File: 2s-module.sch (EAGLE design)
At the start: 3 parts, among them J1 CQ-USB-C16PSMT01

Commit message: build balancer prototype
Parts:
- added C1: 1nF, Capacitor:C_CHIP-0603(1608-METRIC)
- added C2: 22uF, Capacitor:C_CHIP-1206(3216-METRIC)
- added C3, C4, C5: 10nF, Capacitor:C_CHIP-0603(1608-METRIC)
- added JP1: PINHD-1X3, Connector:PINHD-1X3
- added L1: 0630CDMCCDS-4R7MC, 0630CDMCCDS-4R7MC:0630CDMCCDS-4R7MC
- added LED1: red, adafruit:LEDCHIPLED_0603
- added R3: 1k, resistor:R-US_R0603
- added R4: 25k, resistor:R-US_R0603
- added U1: MCP4725, SparkFun-IC-Conversion:MCP4725SOT-23
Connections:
- new net BATC: C4.2, C5.1, JP1.2, L1.P$1, LED1.C, U1.AO
- new net BATP: C2.1, C4.1, JP1.1, U1.SCL
- new net BIAS: C3.2, U1.VDD
- new net ISET: C1.2, R4.2, U1.VOUT
- new net N$1: LED1.A, R3.2
- new net SW: C3.1, L1.P$2, R3.1, U1.SDA
- net GND: now also C1.1, C2.2, C5.2, JP1.3, R4.1, U1.VSS
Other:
- note added: "2.2uH"
- note added: "ETA3000"
- moved on the sheet: R2

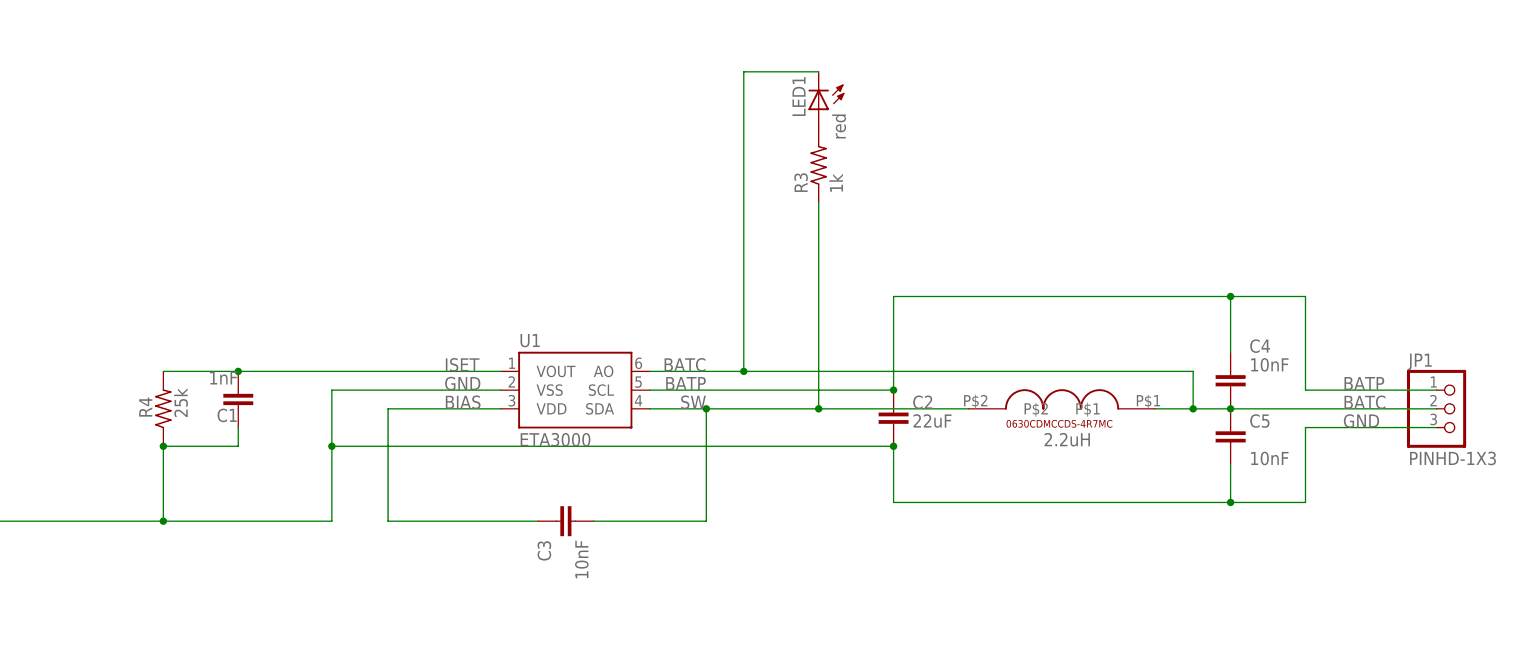
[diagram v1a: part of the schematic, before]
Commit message: add optocoupler
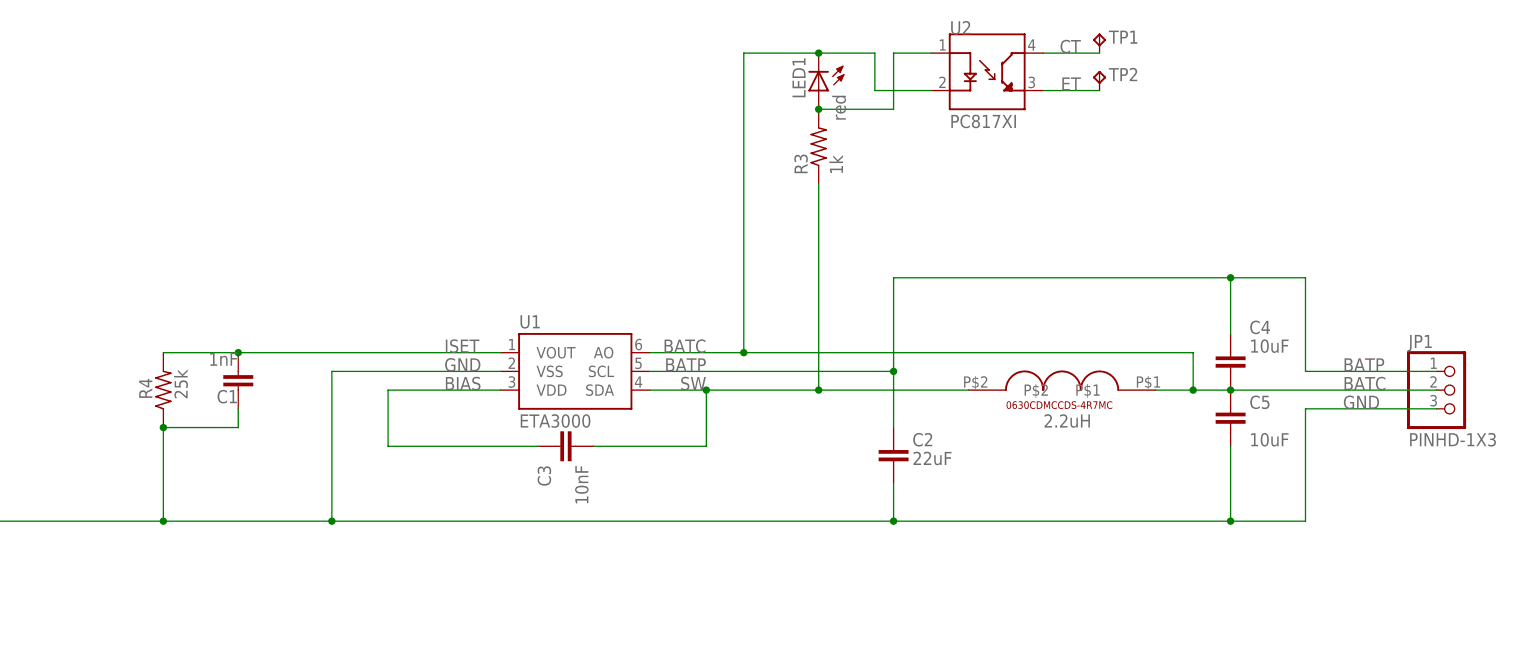
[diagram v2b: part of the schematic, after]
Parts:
- added TP1, TP2: TPB1,27, BeagleBone_Blue_R3:TPB1,27
- added U2: PC817XI, PC817XI:PC817XI
- C4, C5: value 10nF -> 10uF
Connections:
- new net CT: TP1.TP, U2.CT
- new net ET: TP2.TP, U2.ET
- net BATC: now also U2.C
- net N$1: now also U2.A
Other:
- moved on the sheet: C1, C2, C3, C4, C5, JP1, LED1, R3, R4, U1

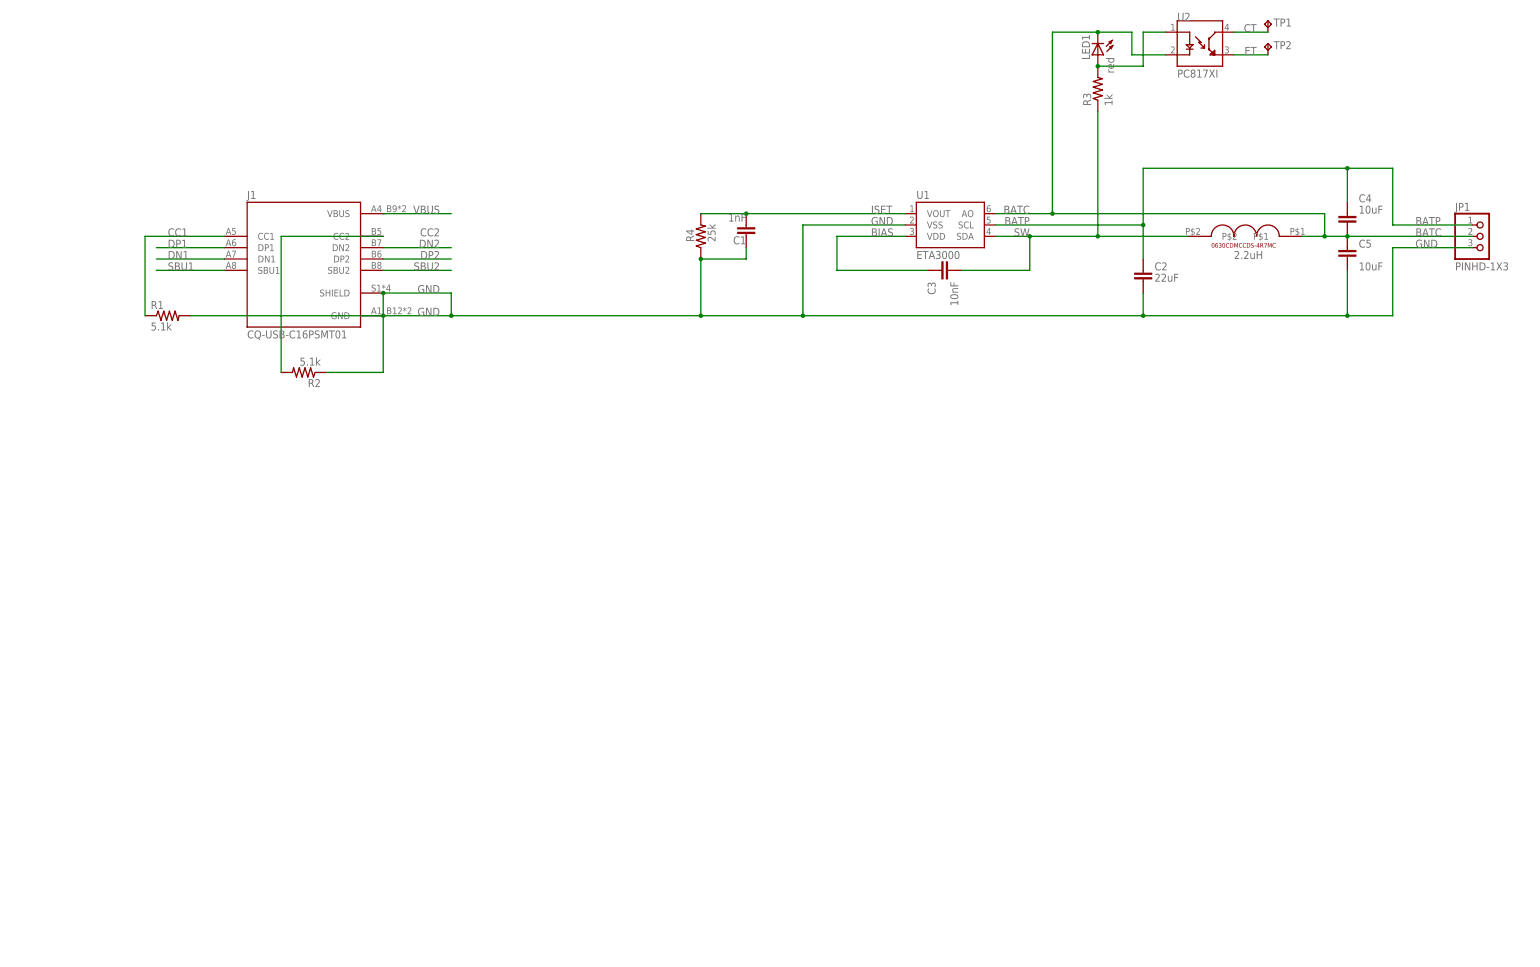
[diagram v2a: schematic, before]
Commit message: finish initial prototype, inductors may change
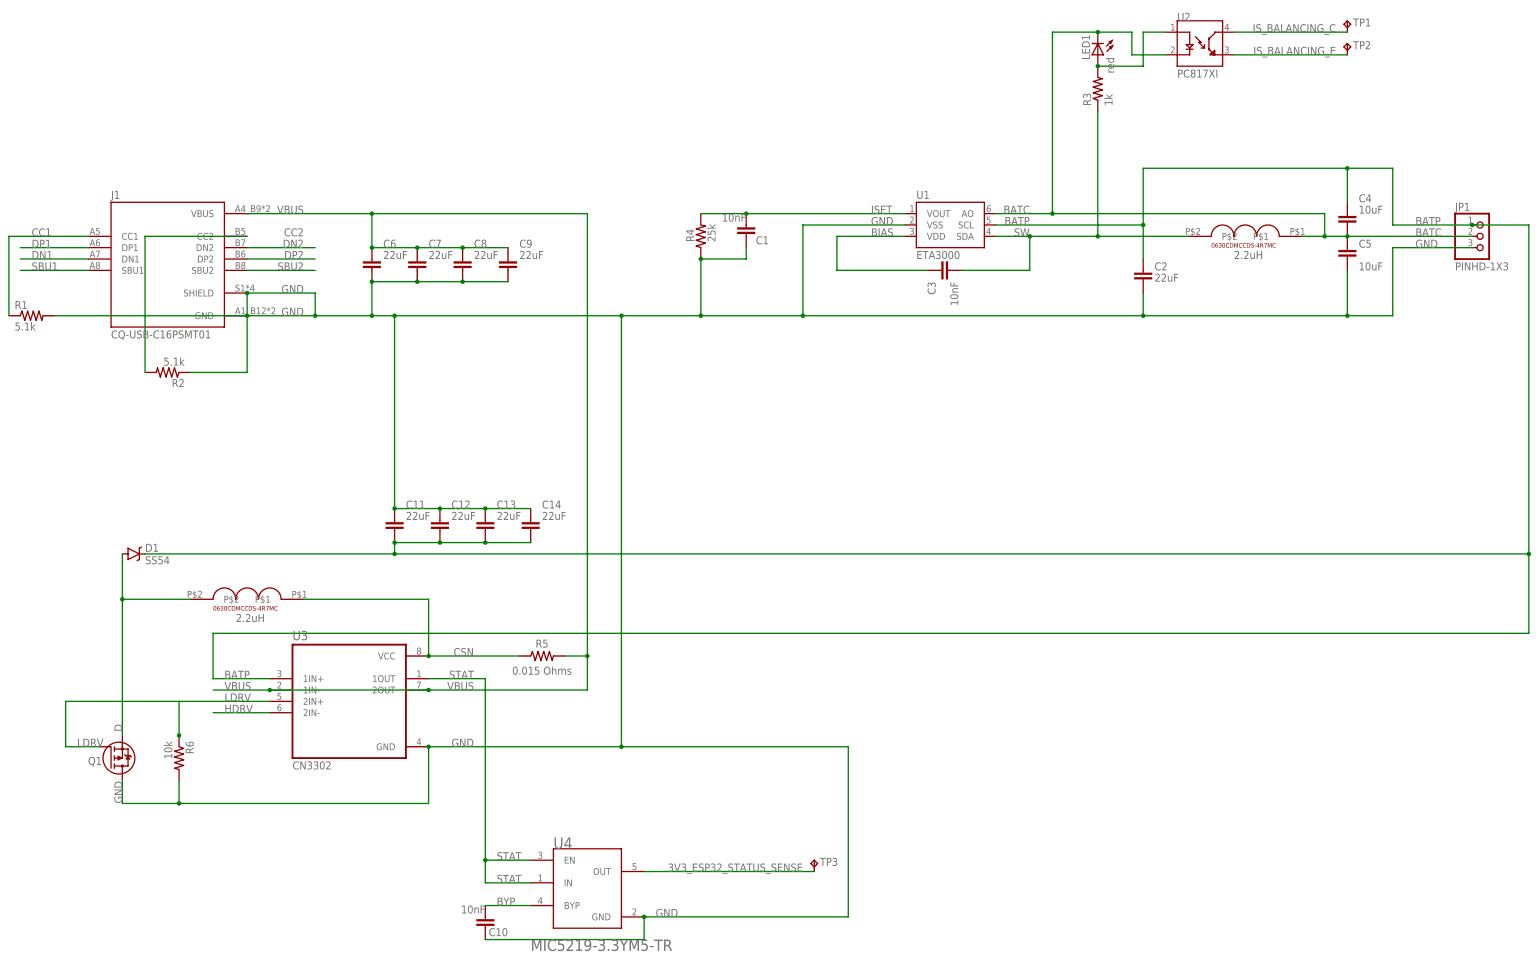
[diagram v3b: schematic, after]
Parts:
- added C10: 10nF, Capacitor:C_CHIP-0603(1608-METRIC)
- added C11, C12, C13, C14, C6, C7, C8, C9: 22uF, Capacitor:C_CHIP-1206(3216-METRIC)
- added D1: SS54, SS54:SS54
- added L2: 0630CDMCCDS-4R7MC, 0630CDMCCDS-4R7MC:0630CDMCCDS-4R7MC
- added Q1: IRFR9020A, semiconductor:IRFR9020A
- added R5: 0.015 Ohms, Resistor:R-US_CHIP-2512(6332-METRIC)
- added R6: 10k, resistor:R-US_R0603
- added TP3: TPB1,27, BeagleBone_Blue_R3:TPB1,27
- added U3: LM393DR, LM393DR:LM393DR
- added U4: MICROCHIP_MIC5219-3_3YM5-TRMICROCHIP_MIC5219-3_3YM5-TR_0_0, Microchip - MIC5219-3.3YM5-TR:MICROCHIP_MIC5219-3_3YM5-TRMICROCHIP_MIC5219-3_3YM5-TR_0_0
- C1: value 1nF -> 10nF
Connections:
- net CT renamed IS_BALANCING_C
- net ET renamed IS_BALANCING_E
- new net 3V3_ESP32_STATUS_SENSE: TP3.TP, U4.OUT
- new net BYP: C10.2, U4.BYP
- new net CSN: L2.P$1, R5.1, U3.VCC
- new net D: D1.A, L2.P$2, Q1.S
- new net HDRV: U3.2IN-
- new net LDRV: Q1.G, R6.1, U3.2IN+
- new net STAT: U3.1OUT, U4.EN, U4.IN
- net BATP: now also C11.2, C12.2, C13.2, C14.2, D1.C, U3.1IN+
- net GND: now also C10.1, C11.1, C12.1, C13.1, C14.1, C6.2, C7.2, C8.2, C9.2, Q1.D, R6.2, U3.GND, U4.GND
- net VBUS: now also C6.1, C7.1, C8.1, C9.1, R5.2, U3.1IN-, U3.2OUT
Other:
- note added: "CN3302"
- moved on the sheet: J1, R1, R2, TP1, TP2

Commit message: fix some parts in sch
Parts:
- added R7: 10k, resistor:R-US_R0603
- R3: value 1k -> var
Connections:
- net 3V3_ESP32_STATUS_SENSE renamed IS_CHARGING_3V3_OUT
- net IS_BALANCING_C renamed IS_BALANCING_C_3V3_IN
- removed net IS_BALANCING_E: TP2.TP, U2.ET
- new net IS_BALANCING_E_GPIO: R7.2, TP2.TP, U2.ET
- net GND: now also R7.1
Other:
- moved on the sheet: C1, C10, C2, C3, C4, C5, C6, C7, C8, C9, J1, JP1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

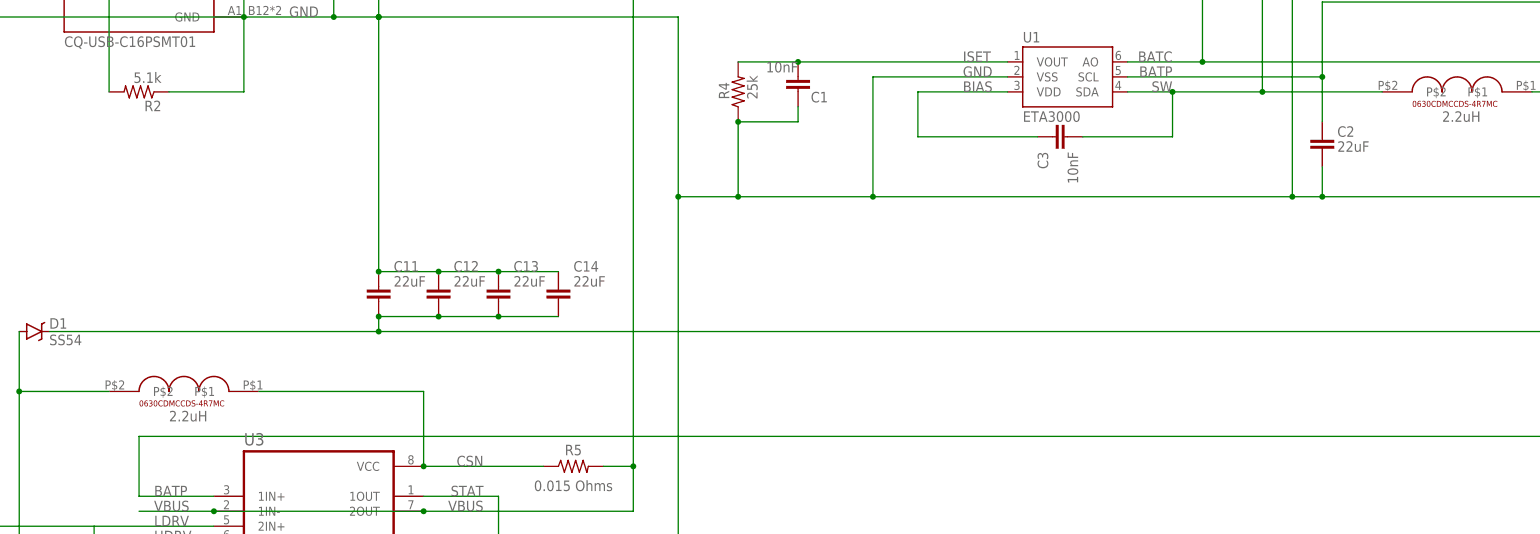
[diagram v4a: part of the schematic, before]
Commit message: add fallback inductor
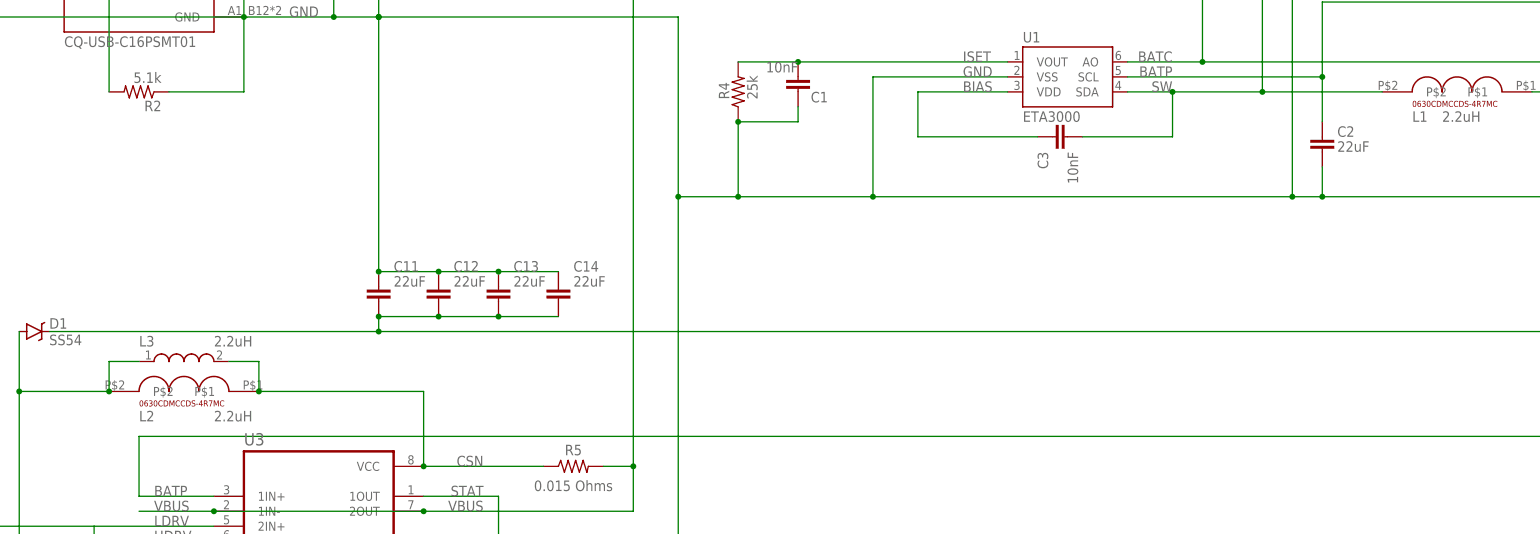
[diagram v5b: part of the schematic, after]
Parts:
- added L3: 2.2uH, 74437368047:74437368047
- L2: value 0630CDMCCDS-4R7MC -> 2.2uH
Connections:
- net CSN: now also L3.2
- net D: now also L3.1
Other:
- note added: "L1"
- note added: "L2"
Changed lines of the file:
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@@
 <part name="C2" library="Capacitor" library_urn="urn:adsk.eagle:library:16290819" deviceset="C" device="CHIP-1206(3216-METRIC)" package3d_urn="urn:adsk.eagle:package:16290893/2" technology="_" value="22uF"/>
 <part name="C3" library="Capacitor" library_urn="urn:adsk.eagle:library:16290819" deviceset="C" device="CHIP-0603(1608-METRIC)" package3d_urn="urn:adsk.eagle:package:16290898/2" technology="_" value="10nF"/>
-<part name="L1" library="0630CDMCCDS-4R7MC" deviceset="0630CDMCCDS-4R7MC" device=""/>
+<part name="L1" library="0630CDMCCDS-4R7MC" deviceset="0630CDMCCDS-4R7MC" device="" value=""/>
 <part name="C4" library="Capacitor" library_urn="urn:adsk.eagle:library:16290819" deviceset="C" device="CHIP-0603(1608-METRIC)" package3d_urn="urn:adsk.eagle:package:16290898/2" technology="_" value="10uF"/>
 <part name="C5" library="Capacitor" library_urn="urn:adsk.eagle:library:16290819" deviceset="C" device="CHIP-0603(1608-METRIC)" package3d_urn="urn:adsk.eagle:package:16290898/2" technology="_" value="10uF"/>
@@
 <part name="R6" library="resistor" library_urn="urn:adsk.eagle:library:348" deviceset="R-US_" device="R0603" package3d_urn="urn:adsk.eagle:package:23555/3" value="10k"/>
 <part name="Q1" library="semiconductor" deviceset="IRFR9020" device="A"/>
-<part name="L2" library="0630CDMCCDS-4R7MC" deviceset="0630CDMCCDS-4R7MC" device=""/>
+<part name="L2" library="0630CDMCCDS-4R7MC" deviceset="0630CDMCCDS-4R7MC" device="" value="2.2uH"/>
 <part name="D1" library="SS54" deviceset="SS54" device=""/>
 <part name="C11" library="Capacitor" library_urn="urn:adsk.eagle:library:16290819" deviceset="C" device="CHIP-1206(3216-METRIC)" package3d_urn="urn:adsk.eagle:package:16290893/2" technology="_" value="22uF"/>
@@
 <part name="C14" library="Capacitor" library_urn="urn:adsk.eagle:library:16290819" deviceset="C" device="CHIP-1206(3216-METRIC)" package3d_urn="urn:adsk.eagle:package:16290893/2" technology="_" value="22uF"/>
 <part name="R7" library="resistor" library_urn="urn:adsk.eagle:library:348" deviceset="R-US_" device="R0603" package3d_urn="urn:adsk.eagle:package:23555/3" value="10k"/>
+<part name="L3" library="74437368047" deviceset="74437368047" device="" value="2.2uH"/>
 </parts>
 <sheets>
@@
 <text x="236.22" y="45.72" size="1.778" layer="96">2.2uH</text>
 <text x="33.02" y="-38.1" size="1.778" layer="95" grouprefs="CHARGER">CN3302</text>
-<text x="20.32" y="-5.08" size="1.778" layer="96" grouprefs="CHARGER">2.2uH</text>
+<text x="27.94" y="-5.08" size="1.778" layer="96" grouprefs="CHARGER">2.2uH</text>
+<text x="231.14" y="45.72" size="1.778" layer="95">L1</text>
+<text x="15.24" y="-5.08" size="1.778" layer="95">L2</text>
 </plain>
 <instances>
@@
 <attribute name="NAME" x="270.2814" y="85.09" size="1.778" layer="95" rot="R90"/>
 <attribute name="VALUE" x="275.082" y="85.09" size="1.778" layer="96" rot="R90"/>
+</instance>
+<instance part="L3" gate="G$1" x="22.86" y="5.08" smashed="yes" rot="R90">
+<attribute name="NAME" x="15.231090625" y="7.624459375" size="1.78111875" layer="95"/>
+<attribute name="VALUE" x="27.942359375" y="7.62118125" size="1.77883125" layer="96"/>
 </instance>
 </instances>
@@
 <wire x1="63.5" y1="0" x2="63.5" y2="-12.7" width="0.1524" layer="91" grouprefs="CHARGER"/>
 <junction x="63.5" y="-12.7" grouprefs="CHARGER"/>
+<pinref part="L3" gate="G$1" pin="2"/>
+<wire x1="30.48" y1="5.08" x2="35.56" y2="5.08" width="0.1524" layer="91"/>
+<wire x1="35.56" y1="5.08" x2="35.56" y2="0" width="0.1524" layer="91"/>
+<junction x="35.56" y="0"/>
 </segment>
 </net>
@@
 <wire x1="-5.08" y1="0" x2="-5.08" y2="10.16" width="0.1524" layer="91" grouprefs="CHARGER"/>
 <junction x="-5.08" y="0" grouprefs="CHARGER"/>
-</segment>
-</net>
+<pinref part="L3" gate="G$1" pin="1"/>
+<wire x1="15.24" y1="5.08" x2="10.16" y2="5.08" width="0.1524" layer="91"/>
+<wire x1="10.16" y1="5.08" x2="10.16" y2="0" width="0.1524" layer="91"/>
+<junction x="10.16" y="0"/>
+</segment>
+</net>
